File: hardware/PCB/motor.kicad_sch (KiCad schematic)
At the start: 50 parts, among them J3 Cutting Tool, U4 BSC050N04LSG

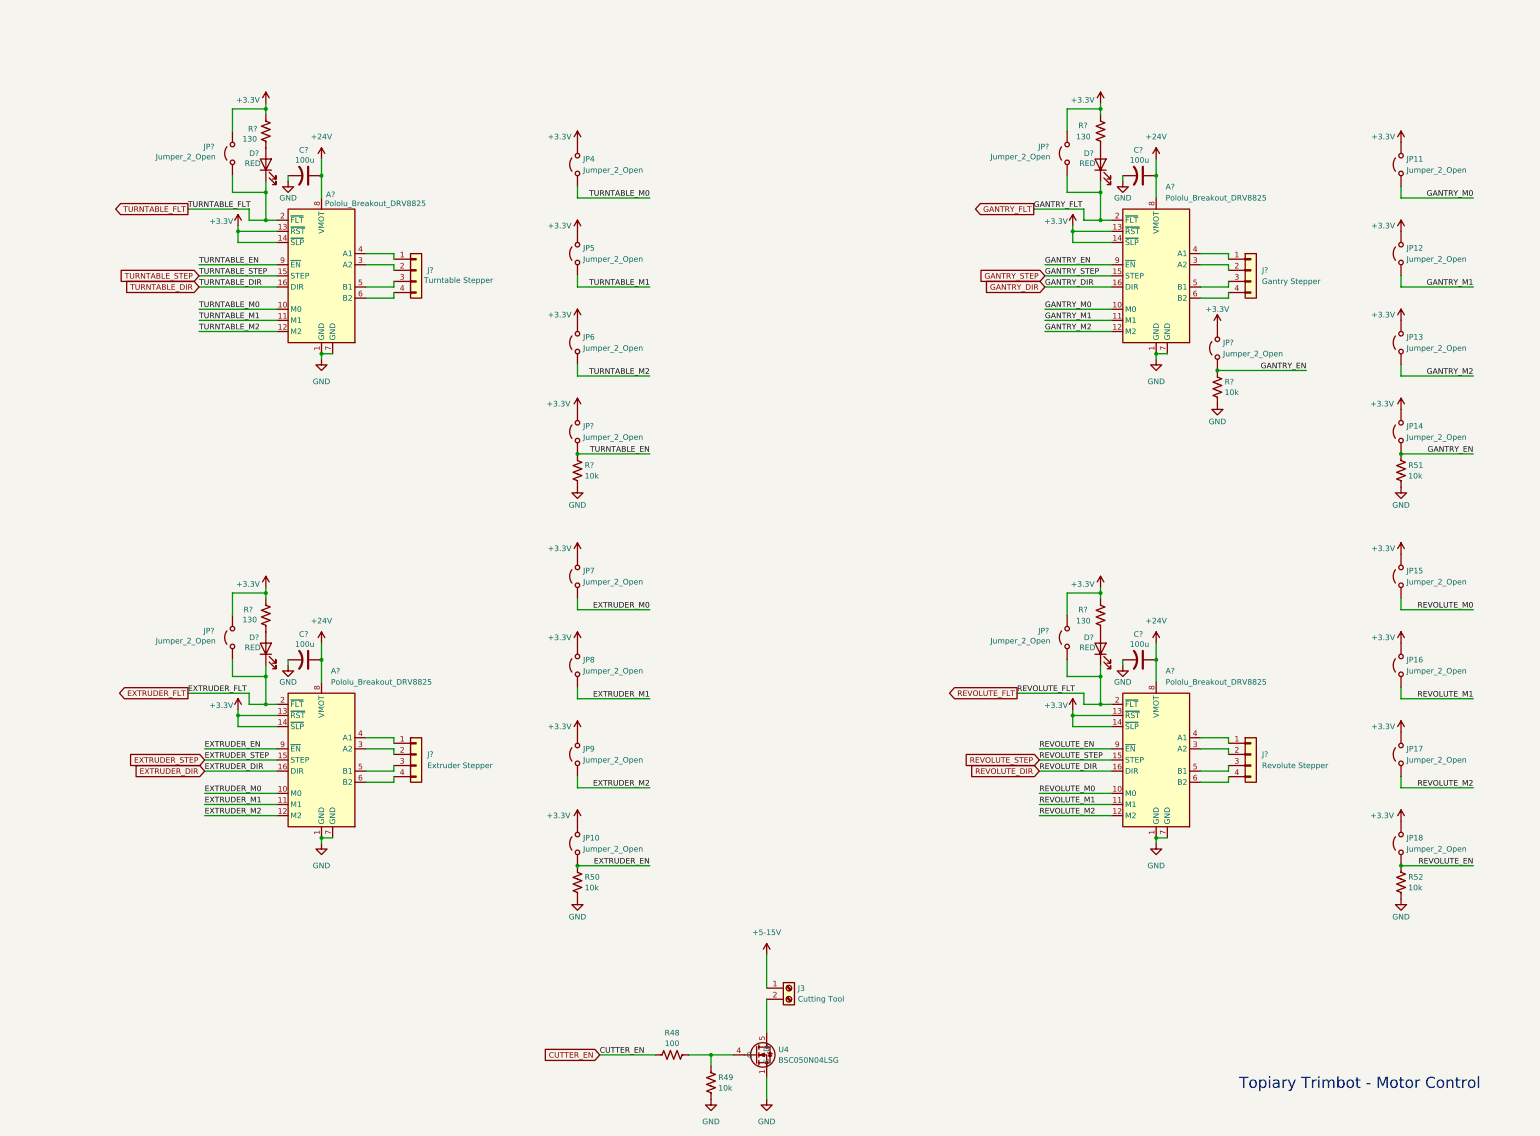
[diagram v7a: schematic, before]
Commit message: Schematic - 24V fan & Driver Test Points
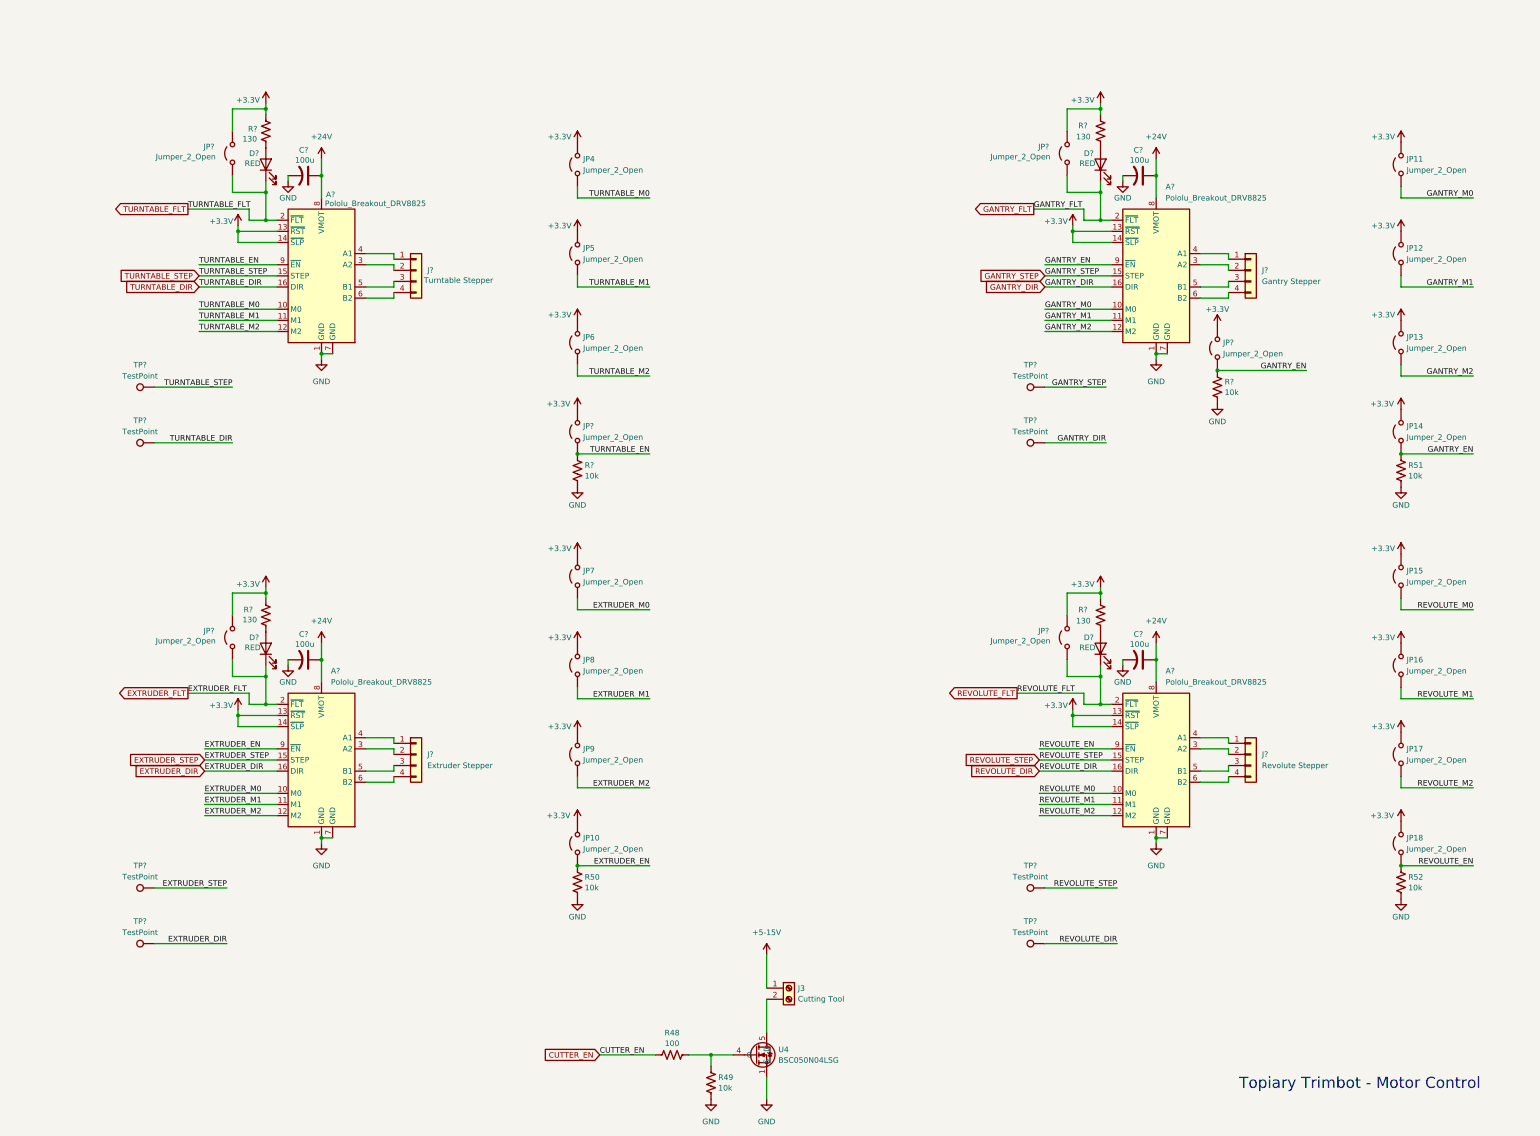
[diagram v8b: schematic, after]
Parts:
- added TP? (x6): TestPoint, symbol Connector:TestPoint
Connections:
- net EXTRUDER_DIR: now also TP?.1
- net EXTRUDER_STEP: now also TP?.1
- net GANTRY_DIR: now also TP?.1
- net GANTRY_STEP: now also TP?.1
- net REVOLUTE_DIR: now also TP?.1
- net REVOLUTE_STEP: now also TP?.1
- net TURNTABLE_DIR: now also TP?.1
- net TURNTABLE_STEP: now also TP?.1
